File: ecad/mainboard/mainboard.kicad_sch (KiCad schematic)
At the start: 46 parts, among them J2 SWD, J3 TYPE-C-31-M-12, J5 UART, SW1 BOOTSEL, SW2 RUN, U2 W25Q128JVS, U22 AMS1117-3.3, U3 RP2040, U4 USBLC6-2SC6, Y1 ABM8-272-T3

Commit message: place parts except analog switches
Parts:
- removed F1: Polyfuse, symbol Device:Polyfuse
- removed U22: AMS1117-3.3, Package_TO_SOT_SMD:SOT-223-3_TabPin2, symbol Regulator_Linear:AMS1117-3.3
- added C16, C17: 1uF, Capacitor_SMD:C_0402_1005Metric, symbol Device:C
- added R12: 560, Resistor_SMD:R_0402_1005Metric, symbol Device:R
- added SW3, SW4: Key_Switch_with_LED, geek_rabb1t:MX_Socket_LED, symbol geek_rabb1t:Key_Switch_with_LED
- added U1: NCP1117-3.3_SOT223, Package_TO_SOT_SMD:SOT-223-3_TabPin2, symbol Regulator_Linear:NCP1117-3.3_SOT223
- added U4: 74AHCT1G125, Package_TO_SOT_SMD:SOT-353_SC-70-5, symbol 74xGxx:74AHCT1G125
- C3: renamed from C18; footprint (none) -> Capacitor_SMD:C_0402_1005Metric
- D1: footprint (none) -> LED_SMD:LED_0603_1608Metric
- J1: renamed from J3; footprint (none) -> Connector_USB:USB_C_Receptacle_HRO_TYPE-C-31-M-12; JLCPCB (none) -> C165948
- J2: symbol Connector:Conn_01x03_Pin -> Connector_Generic_MountingPin:Conn_01x03_MountingPin
- R1: renamed from R26; footprint (none) -> Resistor_SMD:R_0402_1005Metric
- R4: renamed from R27; footprint (none) -> Resistor_SMD:R_0402_1005Metric
- R6: renamed from R10; value R -> 0; footprint (none) -> Resistor_SMD:R_0402_1005Metric
- R7: renamed from R6; footprint (none) -> Resistor_SMD:R_0402_1005Metric
- R8: renamed from R9; footprint (none) -> Resistor_SMD:R_0402_1005Metric
- SW1, SW2: footprint (none) -> Button_Switch_SMD:SW_Push_1P1T_XKB_TS-1187A
- U2: renamed from U4; JLCPCB (none) -> C2827654
- U3: footprint RP2040_minimal:RP2040-QFN-56 -> Package_DFN_QFN:QFN-56-1EP_7x7mm_P0.4mm_EP3.2x3.2mm_ThermalVias
- renumbered J5 to J3, R7 to R2, R8 to R3, R1 to R5
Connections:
- net GPIO10 is gone; now on net GPIO_UNUSED: U3.13 (GPIO10)
- net GPIO11 is gone; now on net GPIO_UNUSED: U3.14 (GPIO11)
- net GPIO12 is gone; now on net GPIO_UNUSED: U3.15 (GPIO12)
- net GPIO13 is gone; now on net GPIO_UNUSED: U3.16 (GPIO13)
- net GPIO14 is gone; now on net GPIO_UNUSED: U3.17 (GPIO14)
- net GPIO15 is gone; now on net GPIO_UNUSED: U3.18 (GPIO15)
- net +3.3V: now also U1.2 (VO)
- net GND: now also C16.2, C17.2, SW3.2, SW3.5 (GND), SW4.2, SW4.5 (GND), U1.1 (GND), U4.1, U4.3 (GND)
- net GPIO_UNUSED: now also U3.41 (GPIO29_ADC3); no longer U3.27 (GPIO16), U3.28 (GPIO17), U3.29 (GPIO18), U3.30 (GPIO19), U3.31 (GPIO20), U3.32 (GPIO21), U3.34 (GPIO22), U3.35 (GPIO23), U3.36 (GPIO24), U3.6 (GPIO4)
- net REF_0.6V: now also U3.6 (GPIO4); no longer U3.41 (GPIO29_ADC3)
- net VBUS: now also J1.A4 (VBUS), J1.A9 (VBUS), J1.B4 (VBUS), J1.B9 (VBUS), C16.1, C17.1, SW3.3 (VDD), SW4.3 (VDD), U1.3 (VI), U4.5 (VCC)
- net ADC0 renamed MUX0_OUT
- net ADC1 renamed MUX1_OUT
- new net: SW3.4 (DOUT), SW4.6 (DIN)
- new net: R12.2, SW3.6 (DIN)
- new net DS_0_IN: SW3.1, U3.34 (GPIO22)
- new net DS_1_IN: SW4.1, U3.35 (GPIO23)
- new net LED_OUT: U3.36 (GPIO24), U4.2
- new net LED_OUT_5V: R12.1, U4.4
- new net MUX0_A: U3.27 (GPIO16)
- new net MUX0_B: U3.28 (GPIO17)
- new net MUX0_C: U3.29 (GPIO18)
- new net MUX1_A: U3.30 (GPIO19)
- new net MUX1_B: U3.31 (GPIO20)
- new net MUX1_C: U3.32 (GPIO21)
- no-connect marks 2 -> 4
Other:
- removed sheet digital_switches
- note added: "Digital switches / LEDs"
- note added: "Input/output capacitors are for NCP1117. Check the datasheet"
- note added: "Keep the output controll pin GND"
- note added: "Make sure C13 is close to pin 45 of RP2040"
- note added: "Make sure C14 is close to pin 44 of RP2040"
- note added: "Make sure R10 and R11 are close to RP2040 (for impedance matching)"
- note removed: "Make sure C10 is close to pin 44 of RP2040"
- note removed: "Make sure C8 is close to pin 45 of RP2040"
- note removed: "Make sure R3 and R4 are close to RP2040 (for impedance matching)"
- moved on the sheet: C17, D1, J2, J3, R8

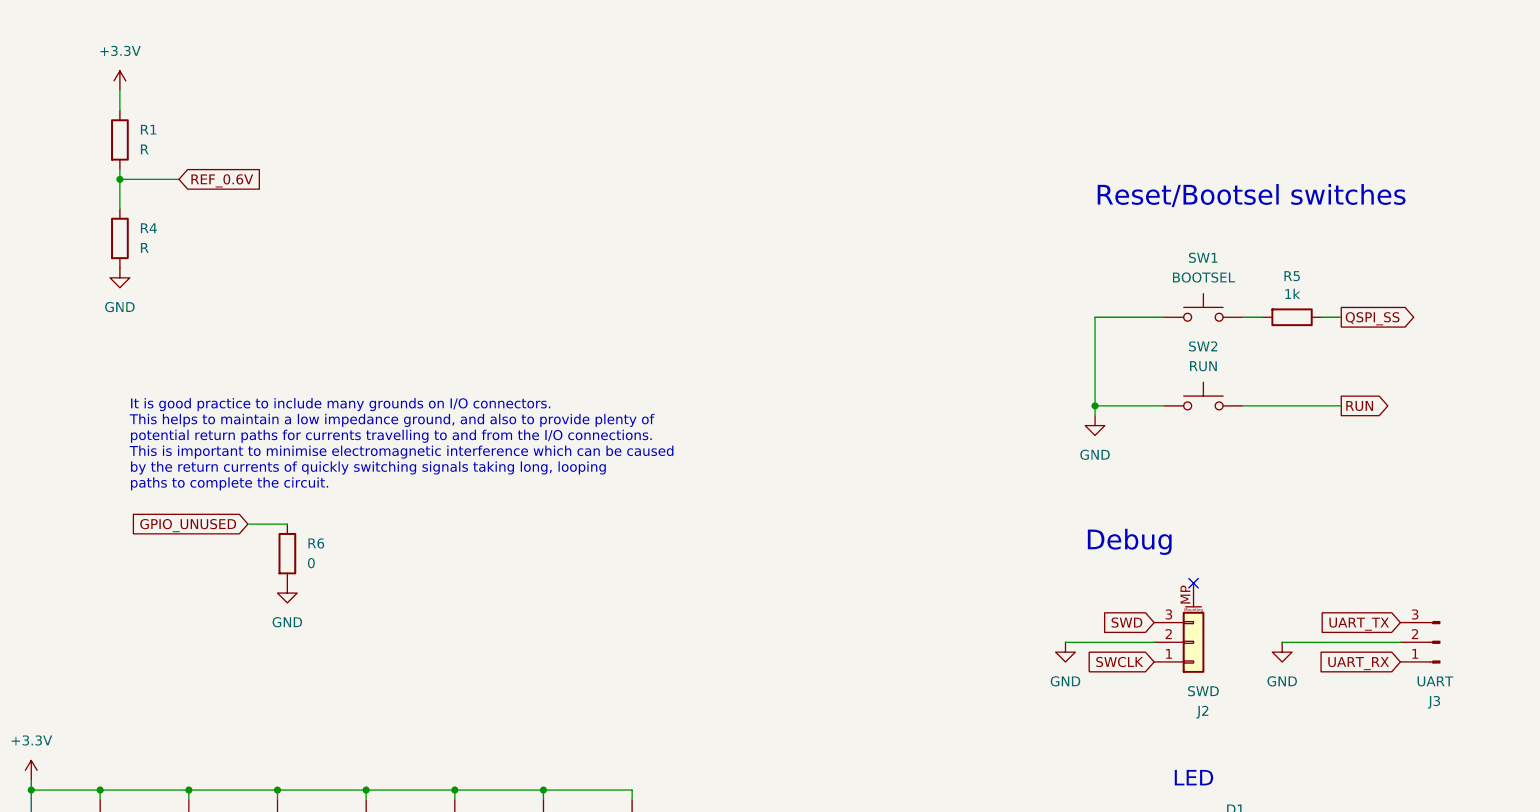
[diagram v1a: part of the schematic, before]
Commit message: fix all DRC errors for connected parts
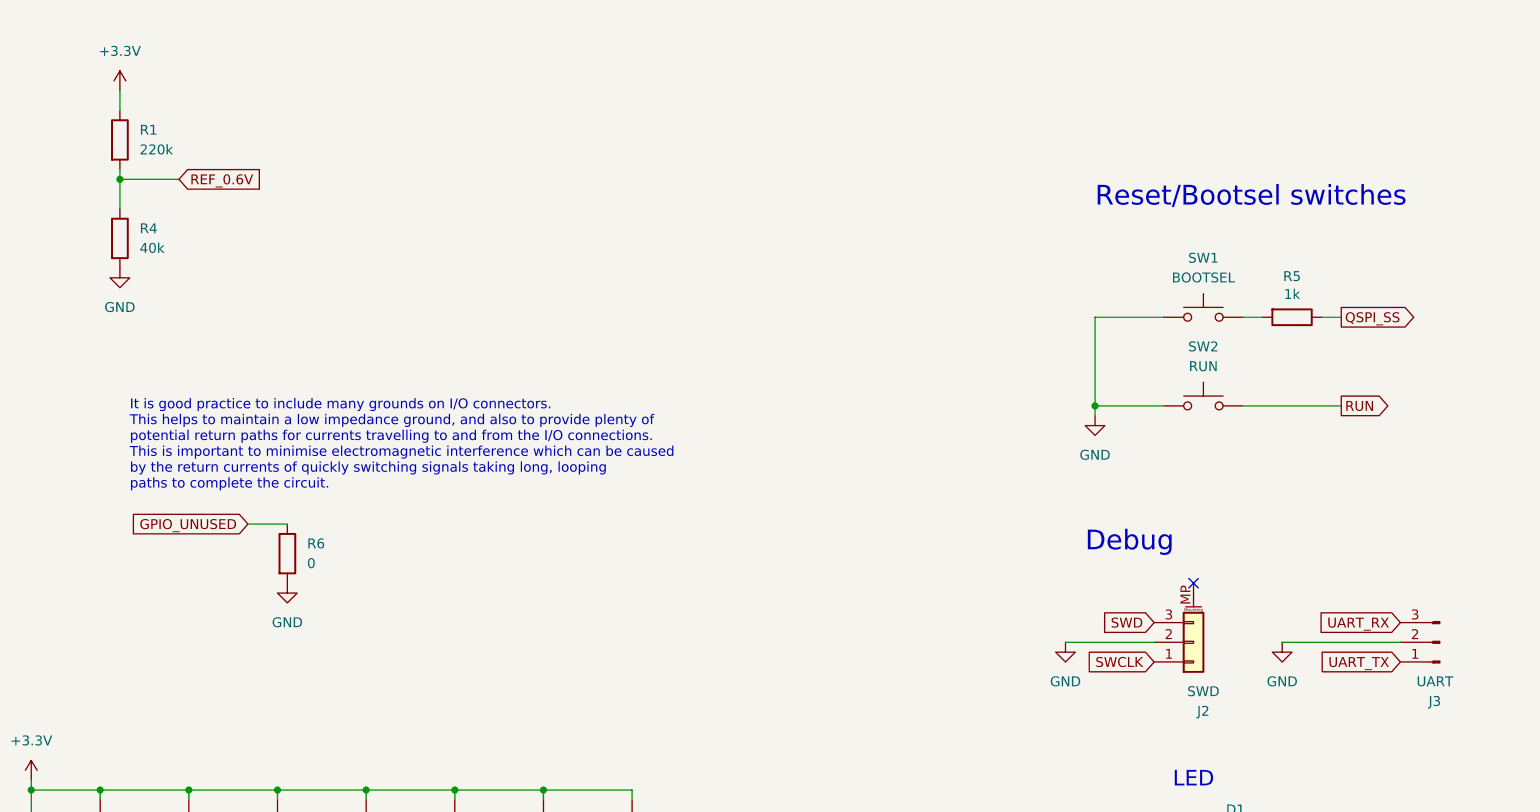
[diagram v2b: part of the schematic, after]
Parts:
- R1: value R -> 220k
- R4: value R -> 40k
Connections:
- net UART_RX: now also J3.3 (Pin_3); no longer J3.1 (Pin_1)
- net UART_TX: now also J3.1 (Pin_1); no longer J3.3 (Pin_3)
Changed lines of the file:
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@@
 	(wire
 		(pts
-			(xy 232.41 82.55) (xy 227.33 82.55)
+			(xy 227.33 82.55) (xy 232.41 82.55)
 		)
 		(stroke
@@
 	(global_label "UART_TX"
 		(shape input)
-		(at 375.92 95.25 180)
+		(at 375.92 100.33 180)
 		(fields_autoplaced yes)
 		(effects
@@
 		)
 		(property "Intersheetrefs" "${INTERSHEET_REFS}"
-			(at 365.1334 95.25 0)
+			(at 365.1334 100.33 0)
 			(effects
 				(font
@@
 	(global_label "UART_RX"
 		(shape input)
-		(at 375.92 100.33 180)
+		(at 375.92 95.25 180)
 		(fields_autoplaced yes)
 		(effects
@@
 		)
 		(property "Intersheetrefs" "${INTERSHEET_REFS}"
-			(at 364.831 100.33 0)
+			(at 364.831 95.25 0)
 			(effects
 				(font
@@
 			)
 		)
-		(property "Value" "R"
+		(property "Value" "220k"
 			(at 213.36 34.2899 0)
 			(effects
@@
 			)
 		)
-		(property "Value" "R"
+		(property "Value" "40k"
 			(at 213.36 46.9899 0)
 			(effects

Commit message: refactor some patterns
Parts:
- added H10, H5, H6, H7, H8, H9: MountingHole, MountingHole:MountingHole_2.7mm_M2.5, symbol Mechanical:MountingHole
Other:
- moved on the sheet: H1, H2, H3, H4

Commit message: Udong board rev.1
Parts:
- removed R6: 0, Resistor_SMD:R_0402_1005Metric, symbol Device:R
- U3: footprint Package_DFN_QFN:QFN-56-1EP_7x7mm_P0.4mm_EP3.2x3.2mm_ThermalVias -> Udong:RP2040-QFN-56
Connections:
- net GPIO_UNUSED is gone; now on net GND: U3.11 (GPIO8), U3.12 (GPIO9), U3.13 (GPIO10), U3.14 (GPIO11), U3.15 (GPIO12), U3.16 (GPIO13), U3.17 (GPIO14), U3.18 (GPIO15), U3.4 (GPIO2), U3.40 (GPIO28_ADC2), U3.41 (GPIO29_ADC3), U3.5 (GPIO3), U3.7 (GPIO5), U3.8 (GPIO6), U3.9 (GPIO7)
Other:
- note added: "This flash strage doesn't require a pull-up registor here (@R9) However, some other device would require a pull-up registor so let me put a DNF registor for the record."

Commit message: .
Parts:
- removed R2: DNF, Resistor_SMD:R_0402_1005Metric, symbol Device:R
- D1: footprint LED_SMD:LED_0603_1608Metric -> LED_SMD:LED_0805_2012Metric; JLCPCB (none) -> C2297
- J2: JLCPCB (none) -> C160403
- SW1: value BOOTSEL -> TS-1187A-B-A-B; JLCPCB (none) -> C318884; フィールド6 (none) -> TS-1187A-B-A-B
- SW2: value RUN -> TS-1187A-B-A-B; JLCPCB (none) -> C318884; フィールド6 (none) -> TS-1187A-B-A-B
- U1: value NCP1117-3.3_SOT223 -> NCP1117ST33T3G
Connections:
- net QSPI_SS is gone; now on net +3.3V: R5.1, U2.1 (~{CS}), U3.56 (QSPI_SS)
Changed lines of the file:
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@@
 	(wire
 		(pts
-			(xy 39.37 149.86) (xy 39.37 160.02)
-		)
-		(stroke
-			(width 0)
-			(type default)
-		)
-	)
-	(wire
-		(pts
 			(xy 337.82 207.01) (xy 337.82 209.55)
 		)
@@
 	(wire
 		(pts
+			(xy 39.37 139.7) (xy 39.37 160.02)
+		)
+		(stroke
+			(width 0)
+			(type default)
+		)
+	)
+	(wire
+		(pts
 			(xy 44.45 72.39) (xy 34.29 72.39)
 		)
@@
 	(wire
 		(pts
-			(xy 39.37 142.24) (xy 39.37 139.7)
-		)
-		(stroke
-			(width 0)
-			(type default)
-		)
-	)
-	(wire
-		(pts
 			(xy 39.37 139.7) (xy 69.85 139.7)
 		)
@@
 	)
 	(symbol
-		(lib_id "Device:R")
-		(at 39.37 146.05 0)
-		(unit 1)
-		(exclude_from_sim no)
-		(in_bom yes)
-		(on_board yes)
-		(dnp no)
-		(property "Reference" "R2"
-			(at 41.148 144.8816 0)
-			(effects
-				(font
-					(size 1.27 1.27)
-				)
-				(justify left)
-			)
-		)
-		(property "Value" "DNF"
-			(at 41.148 147.193 0)
-			(effects
-				(font
-					(size 1.27 1.27)
-				)
-				(justify left)
-			)
-		)
-		(property "Footprint" "Resistor_SMD:R_0402_1005Metric"
-			(at 37.592 146.05 90)
-			(effects
-				(font
-					(size 1.27 1.27)
-				)
-				(hide yes)
-			)
-		)
-		(property "Datasheet" "~"
-			(at 39.37 146.05 0)
-			(effects
-				(font
-					(size 1.27 1.27)
-				)
-				(hide yes)
-			)
-		)
-		(property "Description" ""
-			(at 39.37 146.05 0)
-			(effects
-				(font
-					(size 1.27 1.27)
-				)
-				(hide yes)
-			)
-		)
-		(pin "1"
-		)
-		(pin "2"
-		)
-		(instances
-			(project "RP2040_minimal_r2"
-				(path "/8c0b3d8b-46d3-4173-ab1e-a61765f77d61"
-					(reference "R2")
-					(unit 1)
-				)
-			)
-			(project ""
-				(path "/b1313647-8d60-4294-add7-71c03651cfe3"
-					(reference "R9")
-					(unit 1)
-				)
-			)
-		)
-	)
-	(symbol
 		(lib_id "Device:C")
 		(at 76.2 140.97 0)
@@
 			)
 		)
-		(property "Value" "RUN"
+		(property "Value" "TS-1187A-B-A-B"
 			(at 350.52 62.23 0)
 			(effects
@@
 			)
 		)
+		(property "JLCPCB" "C318884"
+			(at 350.52 67.31 0)
+			(effects
+				(font
+					(size 1.27 1.27)
+				)
+				(hide yes)
+			)
+		)
+		(property "フィールド6" "TS-1187A-B-A-B"
+			(at 350.52 67.31 0)
+			(effects
+				(font
+					(size 1.27 1.27)
+				)
+				(hide yes)
+			)
+		)
 		(pin "1"
 		)
@@
 			)
 		)
+		(property "JLCPCB" "C160403"
+			(at 349.25 97.79 0)
+			(effects
+				(font
+					(size 1.27 1.27)
+				)
+				(hide yes)
+			)
+		)
 		(pin "1"
 		)
@@
 			)
 		)
-		(property "Footprint" "LED_SMD:LED_0603_1608Metric"
+		(property "Footprint" "LED_SMD:LED_0805_2012Metric"
 			(at 353.06 127 0)
 			(effects
@@
 			)
 		)
+		(property "JLCPCB" "C2297"
+			(at 353.06 127 0)
+			(effects
+				(font
+					(size 1.27 1.27)
+				)
+				(hide yes)
+			)
+		)
 		(pin "1"
 		)
@@
 			)
 		)
-		(property "Value" "BOOTSEL"
+		(property "Value" "TS-1187A-B-A-B"
 			(at 350.52 50.8 0)
 			(effects
@@
 			)
 		)
+		(property "JLCPCB" "C318884"
+			(at 350.52 55.88 0)
+			(effects
+				(font
+					(size 1.27 1.27)
+				)
+				(hide yes)
+			)
+		)
+		(property "フィールド6" "TS-1187A-B-A-B"
+			(at 350.52 55.88 0)
+			(effects
+				(font
+					(size 1.27 1.27)
+				)
+				(hide yes)
+			)
+		)
 		(pin "1"
 		)
@@
 			)
 		)
-		(property "Value" "NCP1117-3.3_SOT223"
+		(property "Value" "NCP1117ST33T3G"
 			(at 168.91 33.02 0)
 			(effects

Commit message: add new footprints but broken pcb
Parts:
- removed SW3, SW4: Key_Switch_with_LED, geek_rabb1t:MX_Socket_LED, symbol geek_rabb1t:Key_Switch_with_LED
- added D2, D3: SK6812MINI, Udong:MX_Socket_LED, symbol udong_library:SK6812MINI_1_FIXED
- added R9: 0, symbol Device:R
- added SW3: Digital_Switch_1, symbol Switch:SW_Push
- added SW6: Digital_Switch_2, symbol Switch:SW_Push
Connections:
- net +3.3V: now also R9.2; no longer R5.1, U2.1 (~{CS}), U3.56 (QSPI_SS)
- net DS_0_IN: now also SW3.2
- net DS_1_IN: now also SW6.2
- net GND: now also D2.3 (VSS), D3.3 (VSS), SW3.1, SW6.1
- net VBUS: now also D2.1 (VDD), D3.1 (VDD)
- net at R12.2: now also D2.4 (DIN)
- new net: D2.2 (DOUT), D3.4 (DIN)
- new net QSPI_SS: R5.1, R9.1, U2.1 (~{CS}), U3.56 (QSPI_SS)
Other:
- moved on the sheet: C16, C17, R12

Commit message: .
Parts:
- removed SW6: Digital_Switch_2, symbol Switch:SW_Push
- added SW4: SW_Push, Udong:MX_Socket, symbol Switch:SW_Push
- R9: footprint (none) -> Resistor_SMD:R_0402_1005Metric
- SW3: value Digital_Switch_1 -> SW_Push; footprint (none) -> Udong:MX_Socket
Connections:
- net DS_0_IN: now also SW3.1; no longer SW3.2
- net DS_1_IN: now also SW4.1
- net GND: now also SW3.2, SW4.2; no longer SW3.1
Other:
- moved on the sheet: C16, C17, R12

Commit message: rev1.1
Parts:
- removed R9: 0, Resistor_SMD:R_0402_1005Metric, symbol Device:R
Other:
- note added: "DNF"
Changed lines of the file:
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@@
 		)
 	)
+	(text "DNF\n"
+		(exclude_from_sim no)
+		(at 52.07 139.7 0)
+		(effects
+			(font
+				(size 1.27 1.27)
+			)
+		)
+	)
 	(text "It is good practice to include many grounds on I/O connectors.\nThis helps to maintain a low impedance ground, and also to provide plenty of\npotential return paths for currents travelling to and from the I/O connections.\nThis is important to minimise electromagnetic interference which can be caused \nby the return currents of quickly switching signals taking long, looping\npaths to complete the circuit.\n"
 		(exclude_from_sim no)
@@
 					(unit 1)
 				)
-			)
-		)
-	)
-	(symbol
-		(lib_id "Device:R")
-		(at 52.07 139.7 90)
-		(unit 1)
-		(exclude_from_sim no)
-		(in_bom yes)
-		(on_board yes)
-		(dnp no)
-		(fields_autoplaced yes)
-		(property "Reference" "R9"
-			(at 52.07 133.35 90)
-			(effects
-				(font
-					(size 1.27 1.27)
-				)
-			)
-		)
-		(property "Value" "0"
-			(at 52.07 135.89 90)
-			(effects
-				(font
-					(size 1.27 1.27)
-				)
-			)
-		)
-		(property "Footprint" "Resistor_SMD:R_0402_1005Metric"
-			(at 52.07 141.478 90)
-			(effects
-				(font
-					(size 1.27 1.27)
-				)
-				(hide yes)
-			)
-		)
-		(property "Datasheet" "~"
-			(at 52.07 139.7 0)
-			(effects
-				(font
-					(size 1.27 1.27)
-				)
-				(hide yes)
-			)
-		)
-		(property "Description" "Resistor"
-			(at 52.07 139.7 0)
-			(effects
-				(font
-					(size 1.27 1.27)
-				)
-				(hide yes)
-			)
-		)
-		(pin "2"
-		)
-		(pin "1"
-		)
-		(instances
-			(project ""
-				(path "/b1313647-8d60-4294-add7-71c03651cfe3"
-					(reference "R9")
-					(unit 1)
-				)
